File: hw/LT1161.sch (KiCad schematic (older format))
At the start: 5 parts, among them U501 MOSFET_DRIVER_LT1161, U502 MOSFET_IPG20N04S4L11ATMA1, U503 MOSFET_IPG20N04S4L11ATMA1

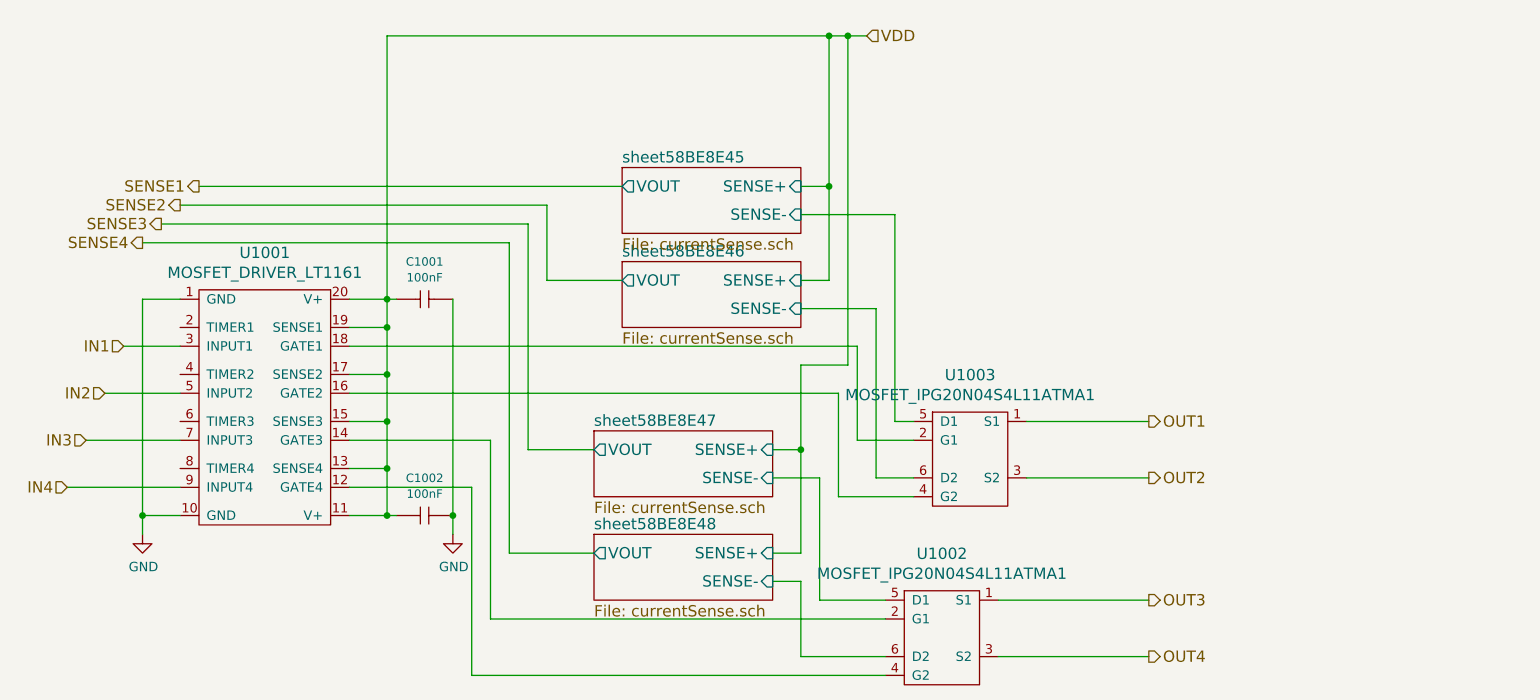
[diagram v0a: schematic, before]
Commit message: added 1k pull down resistors to mosfet gates
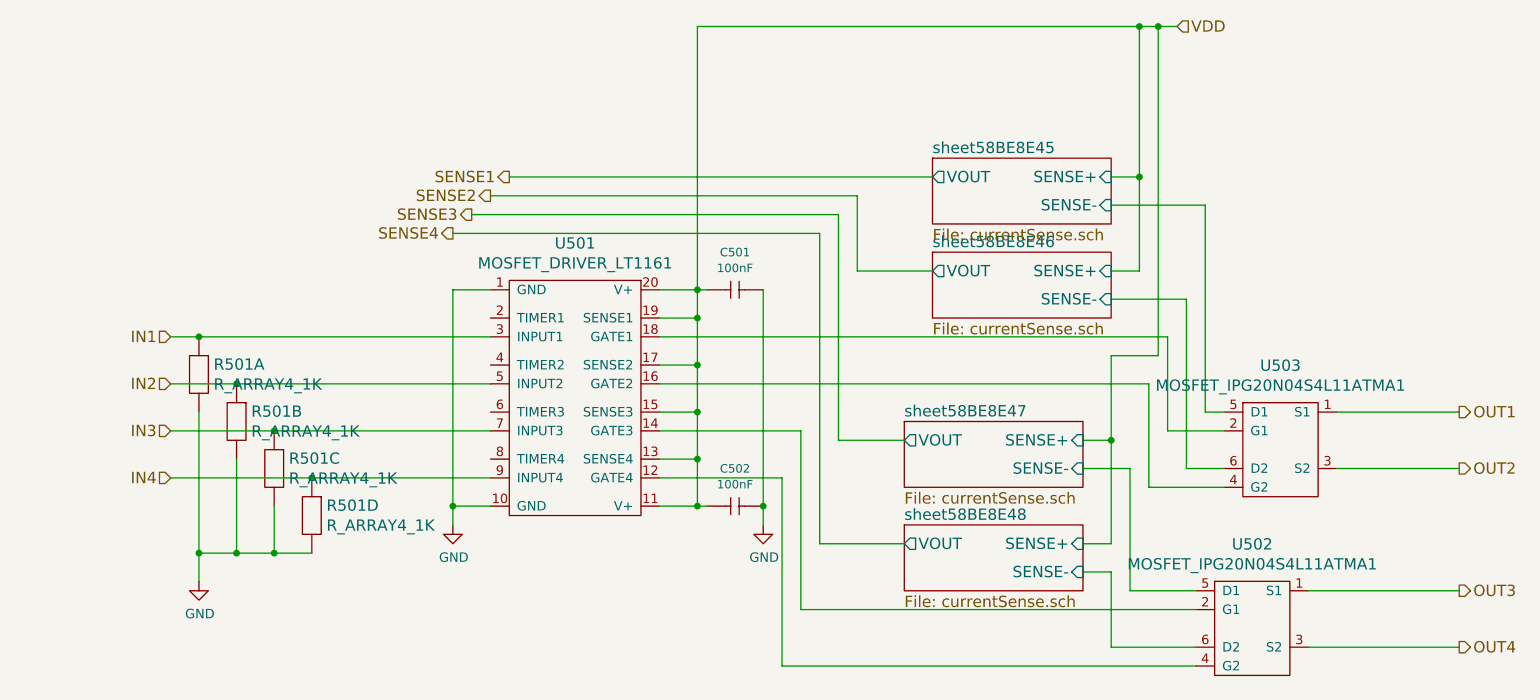
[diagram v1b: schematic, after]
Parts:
- added R501: R_ARRAY4_1K, usevolt:0603_array4, symbol R_ARRAY4_1K
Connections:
- net GND: now also R501.2, R501.4 (2), R501.6 (2), R501.8 (2)
- net IN1: now also R501.1
- net IN2: now also R501.3 (1)
- net IN3: now also R501.5 (1)
- net IN4: now also R501.7 (1)
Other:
- moved on the sheet: C501, C502, U501, U502, U503

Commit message: pcb first revision created, ready to order
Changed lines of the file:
@@
 $Descr A4 11693 8268
 encoding utf-8
-Sheet 5 16
+Sheet 10 18
 Title ""
 Date ""
@@
 AR Path="/58BE52C9/58BE8E62" Ref="#PWR502"  Part="1"
 AR Path="/58C7B0A8/58BE8E62" Ref="#PWR1002"  Part="1"
-F 0 "#PWR502" H 3750 4400 50  0001 C CNN
+F 0 "#PWR1002" H 3750 4400 50  0001 C CNN
 F 1 "GND" H 3755 4477 50  0000 C CNN
 F 2 "" H 3750 4650 50  0000 C CNN
@@
 AR Path="/58BE52C9/58BE8E74" Ref="U501"  Part="1"
 AR Path="/58C7B0A8/58BE8E74" Ref="U1001"  Part="1"
-F 0 "U501" H 4400 4747 60  0000 C CNN
+F 0 "U1001" H 4400 4747 60  0000 C CNN
 F 1 "MOSFET_DRIVER_LT1161" H 4400 4641 60  0000 C CNN
 F 2 "usevolt:SO20" H 4450 4825 60  0001 C CNN
@@
 AR Path="/58BE52C9/58BE8EAF" Ref="C501"  Part="1"
 AR Path="/58C7B0A8/58BE8EAF" Ref="C1001"  Part="1"
-F 0 "C501" H 5250 3599 45  0000 C CNN
+F 0 "C1001" H 5250 3599 45  0000 C CNN
 F 1 "100nF" H 5250 3515 45  0000 C CNN
 F 2 "kemet:0603" H 5230 3550 20  0001 C CNN
@@
 AR Path="/58BE52C9/58BE8EBA" Ref="C502"  Part="1"
 AR Path="/58C7B0A8/58BE8EBA" Ref="C1002"  Part="1"
-F 0 "C502" H 5250 4749 45  0000 C CNN
+F 0 "C1002" H 5250 4749 45  0000 C CNN
 F 1 "100nF" H 5250 4665 45  0000 C CNN
 F 2 "kemet:0603" H 5230 4700 20  0001 C CNN
@@
 AR Path="/58BE52C9/58BE8EC1" Ref="#PWR503"  Part="1"
 AR Path="/58C7B0A8/58BE8EC1" Ref="#PWR1003"  Part="1"
-F 0 "#PWR503" H 5400 4400 50  0001 C CNN
+F 0 "#PWR1003" H 5400 4400 50  0001 C CNN
 F 1 "GND" H 5405 4477 50  0000 C CNN
 F 2 "" H 5400 4650 50  0000 C CNN
@@
 AR Path="/58BE52C9/591C1D78" Ref="U502"  Part="1"
 AR Path="/58C7B0A8/591C1D78" Ref="U1002"  Part="1"
-F 0 "U502" H 8000 5647 60  0000 C CNN
+F 0 "U1002" H 8000 5647 60  0000 C CNN
 F 1 "MOSFET_IPG20N04S4L11ATMA1" H 8000 5541 60  0000 C CNN
 F 2 "usevolt:PG-TDSON-8-4" H 8000 5700 60  0001 C CNN
@@
 AR Path="/58BE52C9/591C1E34" Ref="U503"  Part="1"
 AR Path="/58C7B0A8/591C1E34" Ref="U1003"  Part="1"
-F 0 "U503" H 8150 4697 60  0000 C CNN
+F 0 "U1003" H 8150 4697 60  0000 C CNN
 F 1 "MOSFET_IPG20N04S4L11ATMA1" H 8150 4591 60  0000 C CNN
 F 2 "usevolt:PG-TDSON-8-4" H 8150 4750 60  0001 C CNN
@@
 AR Path="/58BE52C9/593FBF1A" Ref="R501"  Part="1"
 AR Path="/58C7B0A8/593FBF1A" Ref="R1001"  Part="1"
-F 0 "R501" V 2347 3928 60  0000 L CNN
+F 0 "R1001" V 2347 3928 60  0000 L CNN
 F 1 "R_ARRAY4_1K" V 2453 3928 60  0000 L CNN
 F 2 "usevolt:0603_array4" H 2300 3950 60  0001 C CNN
@@
 AR Path="/58BE52C9/593FBFF5" Ref="R501"  Part="2"
 AR Path="/58C7B0A8/593FBFF5" Ref="R1001"  Part="2"
-F 0 "R501" V 2547 4178 60  0000 L CNN
+F 0 "R1001" V 2547 4178 60  0000 L CNN
 F 1 "R_ARRAY4_1K" V 2653 4178 60  0000 L CNN
 F 2 "usevolt:0603_array4" H 2500 4200 60  0001 C CNN
@@
 AR Path="/58BE52C9/593FC0D3" Ref="R501"  Part="3"
 AR Path="/58C7B0A8/593FC0D3" Ref="R1001"  Part="3"
-F 0 "R501" V 2747 4428 60  0000 L CNN
+F 0 "R1001" V 2747 4428 60  0000 L CNN
 F 1 "R_ARRAY4_1K" V 2853 4428 60  0000 L CNN
 F 2 "usevolt:0603_array4" H 2700 4450 60  0001 C CNN
@@
 AR Path="/58BE52C9/593FC1B8" Ref="R501"  Part="4"
 AR Path="/58C7B0A8/593FC1B8" Ref="R1001"  Part="4"
-F 0 "R501" V 2947 4678 60  0000 L CNN
+F 0 "R1001" V 2947 4678 60  0000 L CNN
 F 1 "R_ARRAY4_1K" V 3053 4678 60  0000 L CNN
 F 2 "usevolt:0603_array4" H 2900 4700 60  0001 C CNN
@@
 AR Path="/58BE52C9/593FC6CE" Ref="#PWR501"  Part="1"
 AR Path="/58C7B0A8/593FC6CE" Ref="#PWR1001"  Part="1"
-F 0 "#PWR501" H 2400 4700 50  0001 C CNN
+F 0 "#PWR1001" H 2400 4700 50  0001 C CNN
 F 1 "GND" H 2405 4777 50  0000 C CNN
 F 2 "" H 2400 4950 50  0000 C CNN
